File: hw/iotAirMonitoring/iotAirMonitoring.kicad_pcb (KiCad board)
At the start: 2 copper layers, 0 parts

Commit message: Schematic nearly finished
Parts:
- added C1: 100n, Capacitor_SMD:C_0402_1005Metric, F.Cu at (104.2, 81.4)
- added C10: 22u, Capacitor_SMD:C_0805_2012Metric, F.Cu at (112.0, 92.9)
- added C11: 100n/16V, Capacitor_SMD:C_0402_1005Metric, F.Cu at (106.8, 105.6)
- added C12: 47u/6V3, Capacitor_SMD:C_0805_2012Metric, F.Cu at (105.3, 98.6)
- added C13: 47u/6V3, Capacitor_SMD:C_0805_2012Metric, F.Cu at (112.0, 89.9)
- added C14: 22u, Capacitor_SMD:C_0805_2012Metric, F.Cu at (92.2, 106.9)
- added C15: 22u, Capacitor_SMD:C_0805_2012Metric, F.Cu at (112.0, 86.9)
- added C16: 4u7/16V, Capacitor_SMD:C_0603_1608Metric, F.Cu at (105.1, 101.4)
- added C17: 4u7/16V, Capacitor_SMD:C_0603_1608Metric, F.Cu at (109.6, 98.4)
- added C18: 10n/50V, Capacitor_SMD:C_0402_1005Metric, F.Cu at (106.8, 103.6)
- added C19: 1n, Capacitor_SMD:C_0402_1005Metric, F.Cu at (103.3, 107.6)
- added C2: 22u, Capacitor_SMD:C_0805_2012Metric, F.Cu at (100.5, 80.4)
- added C20: 47p, Capacitor_SMD:C_0402_1005Metric, F.Cu at (111.5, 100.6)
- added C21: 10n, Capacitor_SMD:C_0402_1005Metric, F.Cu at (113.0, 97.4)
- added C3: 100n, Capacitor_SMD:C_0402_1005Metric, F.Cu at (121.5, 76.4)
- added C4: 100n, Capacitor_SMD:C_0402_1005Metric, F.Cu at (132.7, 65.3)
- added C5: 100n, Capacitor_SMD:C_0402_1005Metric, F.Cu at (136.5, 60.7)
- added C6: 1n, Capacitor_SMD:C_0402_1005Metric, F.Cu at (118.5, 80.0)
- added C7: 100n, Capacitor_SMD:C_0402_1005Metric, F.Cu at (139.1, 58.8)
- added C8: 100n, Capacitor_SMD:C_0402_1005Metric, F.Cu at (107.1, 81.4)
- added C9: 22u, Capacitor_SMD:C_0805_2012Metric, F.Cu at (96.7, 106.9)
- added D1: LED, LED_SMD:LED_0805_2012Metric_Pad1.15x1.40mm_HandSolder, F.Cu at (96.1, 77.3)
- added D2: LED, LED_SMD:LED_0805_2012Metric_Pad1.15x1.40mm_HandSolder, F.Cu at (91.3, 77.3)
- added D3: LED, LED_SMD:LED_0805_2012Metric_Pad1.15x1.40mm_HandSolder, F.Cu at (86.5, 77.3)
- added D4: LED, LED_SMD:LED_0805_2012Metric_Pad1.15x1.40mm_HandSolder, F.Cu at (100.9, 77.3)
- added D5: SS54, Diode_SMD:D_SMA, F.Cu at (79.6, 105.7)
- added H1: MountingHole, MountingHole:MountingHole_3.2mm_M3_Pad_Via, F.Cu at (125.2, 87.0)
- added H2: MountingHole, MountingHole:MountingHole_3.2mm_M3_Pad_Via, F.Cu at (133.2, 87.0)
- added H3: MountingHole, MountingHole:MountingHole_3.2mm_M3_Pad_Via, F.Cu at (125.2, 95.0)
- added H4: MountingHole, MountingHole:MountingHole_3.2mm_M3_Pad_Via, F.Cu at (133.2, 95.0)
- added J1: MQ-7, Connector_PinSocket_2.54mm:PinSocket_1x04_P2.54mm_Vertical, F.Cu at (121.3, 45.6)
- added J10: USB_DATA, Connector_PinHeader_2.54mm:PinHeader_1x02_P2.54mm_Vertical, F.Cu at (107.4, 87.7)
- added J11: PWR, Connector_PinHeader_2.54mm:PinHeader_1x02_P2.54mm_Vertical, F.Cu at (96.3, 96.0)
- added J12: USB_B_Micro, Connector_USB:USB_Micro-B_Amphenol_10118194_Horizontal, F.Cu at (80.6, 99.0)
- added J2: VEML7700, Connector_PinSocket_2.54mm:PinSocket_1x05_P2.54mm_Vertical, F.Cu at (112.1, 45.6)
- added J3: SHT40, Connector_PinSocket_2.54mm:PinSocket_1x04_P2.54mm_Vertical, F.Cu at (116.7, 45.6)
- added J4: PROGRAMMER, Connector_PinHeader_2.54mm:PinHeader_1x06_P2.54mm_Vertical, F.Cu at (118.9, 85.3)
- added J5: ML8511, Connector_PinSocket_2.54mm:PinSocket_1x05_P2.54mm_Vertical, F.Cu at (107.5, 68.0)
- added J6: EN_3V3_PROGRAMMER, Connector_PinHeader_2.54mm:PinHeader_1x02_P2.54mm_Vertical, F.Cu at (139.4, 85.3)
- added J7: BMP388, Connector_PinSocket_2.54mm:PinSocket_1x08_P2.54mm_Vertical, F.Cu at (107.5, 45.6)
- added J9: USB_C_Receptacle_USB2.0, Connector_USB:USB_C_Receptacle_HRO_TYPE-C-31-M-12, F.Cu at (81.5, 91.2)
- added JP1: EN, Jumper:SolderJumper-2_P1.3mm_Open_RoundedPad1.0x1.5mm, F.Cu at (111.9, 79.8)
- added JP2: EN, Jumper:SolderJumper-2_P1.3mm_Open_RoundedPad1.0x1.5mm, F.Cu at (136.3, 53.6)
- added JP3: EN, Jumper:SolderJumper-2_P1.3mm_Open_RoundedPad1.0x1.5mm, F.Cu at (116.4, 75.2)
- added L1: 4u7, Inductor_SMD:L_Bourns-SRN6028, F.Cu at (101.1, 89.1)
- added Q1: MMBT3904, Package_TO_SOT_SMD:SOT-23, F.Cu at (127.0, 62.6)
- added Q10: AO3401A, Package_TO_SOT_SMD:SOT-23, F.Cu at (107.3, 94.9)
- added Q11: 2N7002, Package_TO_SOT_SMD:SOT-23, F.Cu at (100.9, 99.7)
- added Q12: AO3401A, Package_TO_SOT_SMD:SOT-23, F.Cu at (87.8, 104.6)
- added Q13: 2N7002, Package_TO_SOT_SMD:SOT-23, F.Cu at (96.2, 103.1)
- added Q2: MMBT3904, Package_TO_SOT_SMD:SOT-23, F.Cu at (122.5, 67.2)
- added Q3: AO3401A, Package_TO_SOT_SMD:SOT-23, F.Cu at (122.5, 62.6)
- added Q4: 2N7002, Package_TO_SOT_SMD:SOT-23, F.Cu at (112.0, 71.2)
- added Q5: AO3401A, Package_TO_SOT_SMD:SOT-23, F.Cu at (116.4, 71.2)
- added Q6: 2N7002, Package_TO_SOT_SMD:SOT-23, F.Cu at (112.0, 75.7)
- added Q7: AO3401A, Package_TO_SOT_SMD:SOT-23, F.Cu at (116.6, 57.8)
- added Q8: 2N7002, Package_TO_SOT_SMD:SOT-23, F.Cu at (121.0, 57.8)
- added Q9: AO3401A, Package_TO_SOT_SMD:SOT-23, F.Cu at (100.9, 95.2)
- added R1: R, Resistor_SMD:R_0805_2012Metric_Pad1.20x1.40mm_HandSolder, F.Cu at (91.2, 80.3)
- added R10: 10k, Resistor_SMD:R_0402_1005Metric, F.Cu at (129.8, 65.9)
- added R11: 220, Resistor_SMD:R_0402_1005Metric, F.Cu at (118.6, 78.0)
- added R12: 220, Resistor_SMD:R_0402_1005Metric, F.Cu at (122.9, 74.4)
- added R13: 100k, Resistor_SMD:R_0402_1005Metric, F.Cu at (133.6, 63.4)
- added R14: 3k3, Resistor_SMD:R_0402_1005Metric, F.Cu at (139.1, 56.8)
- added R15: 330, Resistor_SMD:R_0402_1005Metric, F.Cu at (126.2, 69.5)
- added R16: 3k3, Resistor_SMD:R_0402_1005Metric, F.Cu at (125.9, 71.5)
- added R17: 100k, Resistor_SMD:R_0402_1005Metric, F.Cu at (142.8, 54.8)
- added R18: 220, Resistor_SMD:R_0402_1005Metric, F.Cu at (139.9, 54.8)
- added R19: 220, Resistor_SMD:R_0402_1005Metric, F.Cu at (129.1, 69.5)
- added R2: R, Resistor_SMD:R_0805_2012Metric_Pad1.20x1.40mm_HandSolder, F.Cu at (95.9, 80.3)
- added R20: 100k, Resistor_SMD:R_0402_1005Metric, F.Cu at (142.8, 52.8)
- added R21: R, Resistor_SMD:R_0805_2012Metric_Pad1.20x1.40mm_HandSolder, F.Cu at (86.4, 80.3)
- added R22: 100k, Resistor_SMD:R_0402_1005Metric, F.Cu at (115.6, 80.0)
- added R23: 220, Resistor_SMD:R_0402_1005Metric, F.Cu at (123.0, 72.5)
- added R24: 100k, Resistor_SMD:R_0402_1005Metric, F.Cu at (115.7, 78.0)
- added R25: 100k, Resistor_SMD:R_0402_1005Metric, F.Cu at (123.0, 70.5)
- added R26: 100k, Resistor_SMD:R_0402_1005Metric, F.Cu at (120.0, 74.5)
- added R27: 5k1, Resistor_SMD:R_0402_1005Metric, F.Cu at (100.4, 105.5)
- added R28: 5k1, Resistor_SMD:R_0402_1005Metric, F.Cu at (111.0, 95.4)
- added R29: 100k, Resistor_SMD:R_0402_1005Metric, F.Cu at (113.9, 95.4)
- added R3: 1k, Resistor_SMD:R_0402_1005Metric, F.Cu at (120.1, 72.5)
- added R30: 100k, Resistor_SMD:R_0402_1005Metric, F.Cu at (103.3, 105.6)
- added R31: 10k, Resistor_SMD:R_0402_1005Metric, F.Cu at (108.6, 101.1)
- added R32: 100k, Resistor_SMD:R_0402_1005Metric, F.Cu at (103.9, 103.7)
- added R33: 100k, Resistor_SMD:R_0402_1005Metric, F.Cu at (100.4, 107.5)
- added R34: 15k, Resistor_SMD:R_0402_1005Metric, F.Cu at (91.5, 103.3)
- added R35: 4k7, Resistor_SMD:R_0402_1005Metric, F.Cu at (88.8, 94.6)
- added R36: 100k, Resistor_SMD:R_0402_1005Metric, F.Cu at (91.7, 94.6)
- added R37: 30k, Resistor_SMD:R_0603_1608Metric, F.Cu at (100.5, 103.3)
- added R4: 1k, Resistor_SMD:R_0402_1005Metric, F.Cu at (139.9, 52.8)
- added R5: 1k, Resistor_SMD:R_0402_1005Metric, F.Cu at (111.2, 59.0)
- added R6: 10k, Resistor_SMD:R_0402_1005Metric, F.Cu at (130.7, 63.4)
- added R7: 220, Resistor_SMD:R_0402_1005Metric, F.Cu at (130.7, 61.4)
- added R8: 10k, Resistor_SMD:R_0402_1005Metric, F.Cu at (133.6, 61.4)
- added R9: 220, Resistor_SMD:R_0402_1005Metric, F.Cu at (120.1, 70.5)
- added SW1: SW_Push, Button_Switch_THT:SW_PUSH_6mm, F.Cu at (111.8, 62.4)
- added SW2: SW_Push, Button_Switch_THT:SW_PUSH_6mm, F.Cu at (125.6, 53.8)
- added SW3: RESET, Button_Switch_THT:SW_PUSH_6mm, F.Cu at (125.6, 45.3)
- added SW4: SW_Push, Button_Switch_THT:SW_PUSH_6mm, F.Cu at (136.1, 45.3)
- added TP1: TP_SDA, TestPoint:TestPoint_Pad_D1.5mm, F.Cu at (126.5, 66.7)
- added TP2: TP_SCL, TestPoint:TestPoint_Pad_D1.5mm, F.Cu at (135.9, 57.1)
- added U1: ESP32-WROOM-32, RF_Module:ESP32-WROOM-32, F.Cu at (90.4, 64.8)
- added U2: MCP3202-BI/SN, Package_SO:SOIC-8_3.9x4.9mm_P1.27mm, F.Cu at (79.8, 79.0)
- added U3: AMS1117-3.3, Package_TO_SOT_SMD:SOT-223-3_TabPin2, F.Cu at (92.2, 89.5)
- added U4: TPS54331, Package_SO:SOIC-8_3.9x4.9mm_P1.27mm, F.Cu at (89.8, 99.1)

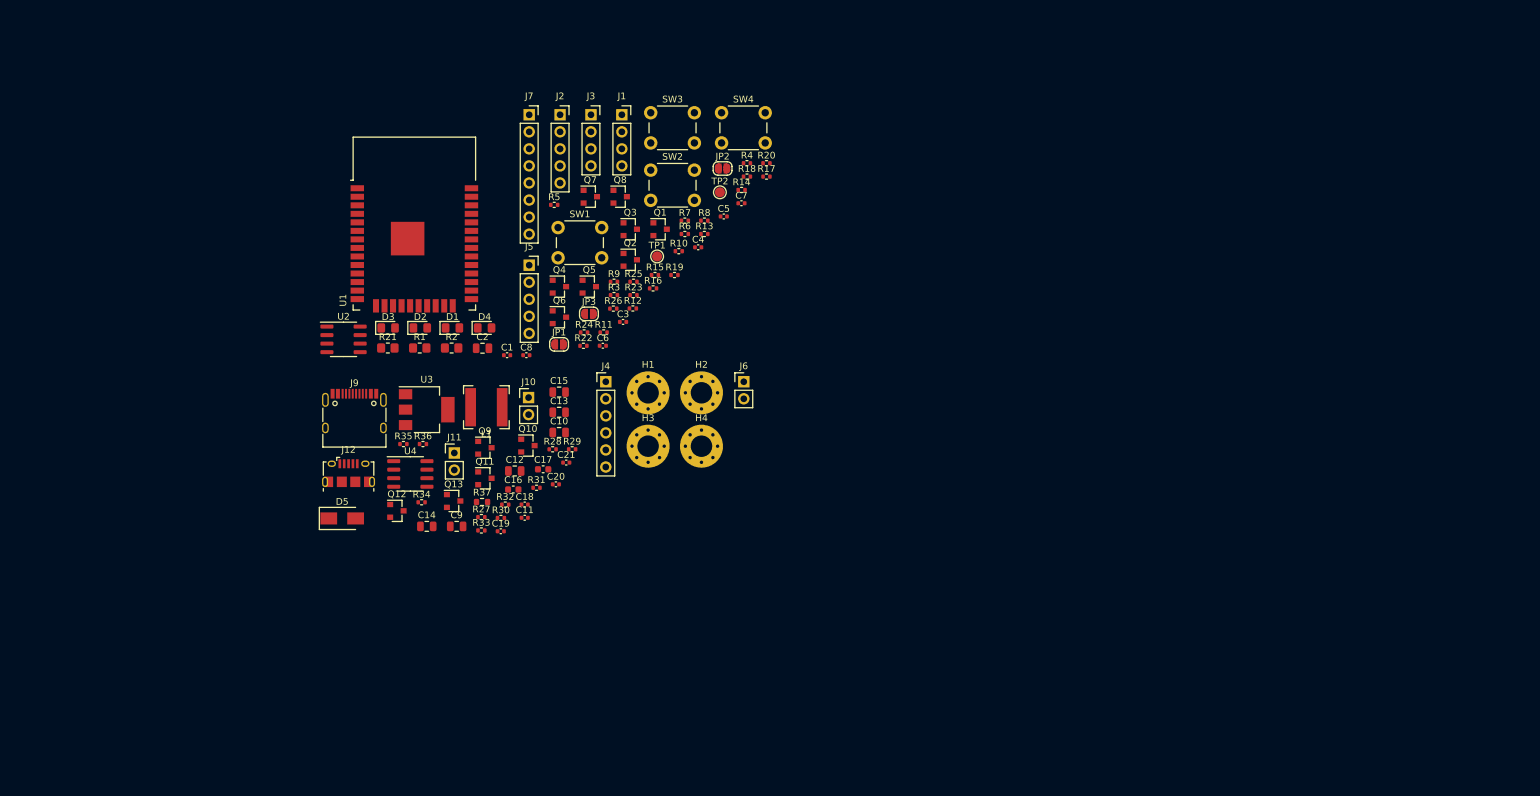
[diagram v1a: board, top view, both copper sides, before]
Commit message: Start routing main board
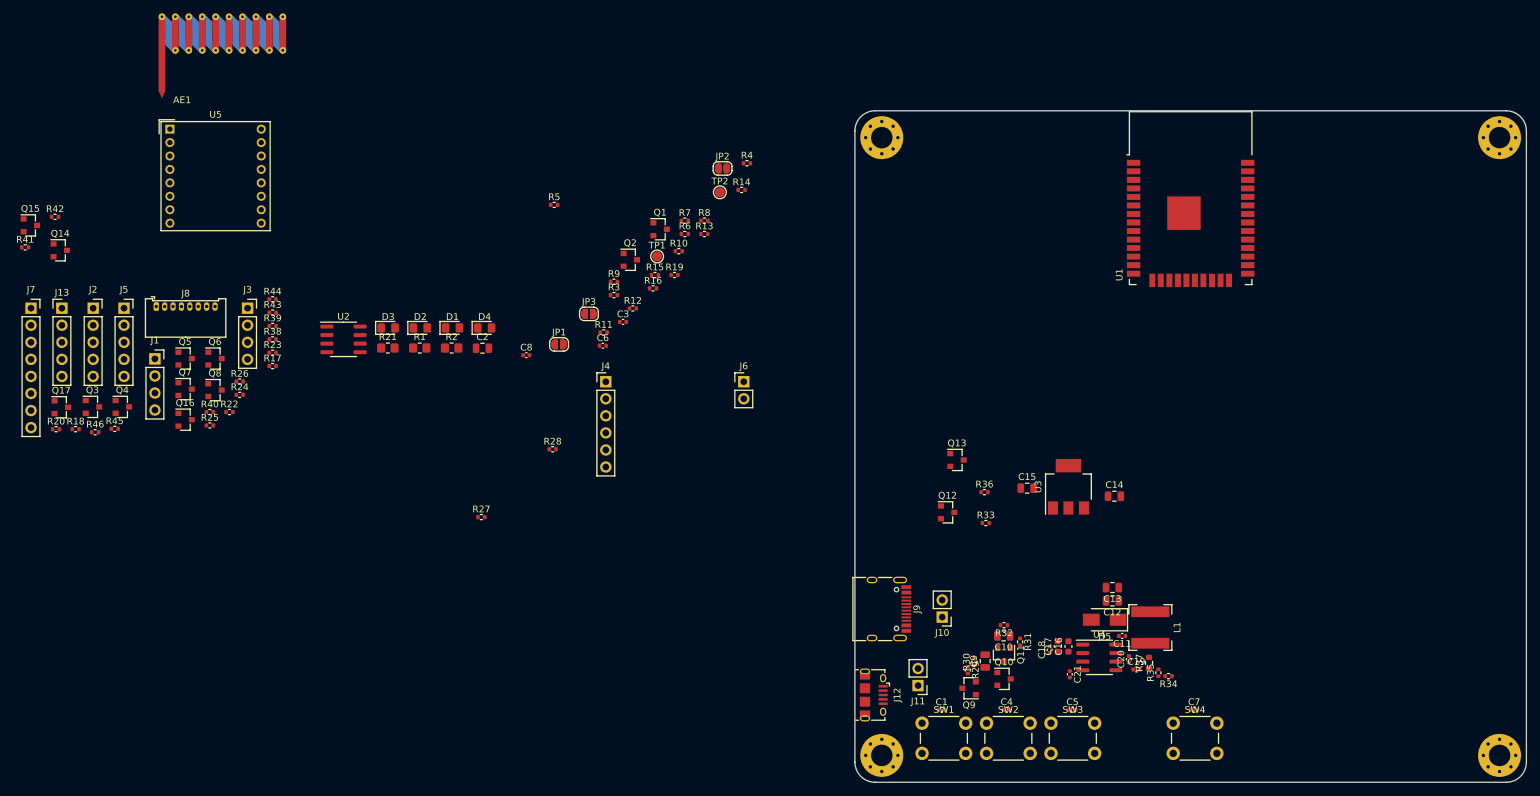
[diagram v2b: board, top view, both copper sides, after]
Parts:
- added AE1: Antenna, RF_Antenna:Texas_SWRA416_868MHz_915MHz, F.Cu at (61.8, 36.8)
- added J13: PM1003, Connector_PinHeader_2.54mm:PinHeader_1x05_P2.54mm_Vertical, F.Cu at (37.9, 74.4)
- added J8: PMS5003, Connector_Molex:Molex_PicoBlade_53048-0810_1x08_P1.25mm_Horizontal, F.Cu at (52.0, 74.2)
- added Q14: AO3401A, Package_TO_SOT_SMD:SOT-23, F.Cu at (37.6, 65.8)
- added Q15: 2N7002, Package_TO_SOT_SMD:SOT-23, F.Cu at (33.2, 62.1)
- added Q16: 2N7002, Package_TO_SOT_SMD:SOT-23, F.Cu at (56.2, 91.0)
- added Q17: 2N7002, Package_TO_SOT_SMD:SOT-23, F.Cu at (37.8, 89.2)
- added R38: 100k, Resistor_SMD:R_0402_1005Metric, F.Cu at (69.3, 79.0)
- added R39: 100k, Resistor_SMD:R_0402_1005Metric, F.Cu at (69.3, 77.0)
- added R40: 100k, Resistor_SMD:R_0402_1005Metric, F.Cu at (59.9, 89.9)
- added R41: 100k, Resistor_SMD:R_0402_1005Metric, F.Cu at (32.4, 65.3)
- added R42: 100k, Resistor_SMD:R_0402_1005Metric, F.Cu at (36.9, 60.8)
- added R43: 100k, Resistor_SMD:R_0402_1005Metric, F.Cu at (69.3, 75.1)
- added R44: 100k, Resistor_SMD:R_0402_1005Metric, F.Cu at (69.3, 73.1)
- added R45: 100k, Resistor_SMD:R_0402_1005Metric, F.Cu at (45.8, 92.4)
- added R46: 100k, Resistor_SMD:R_0402_1005Metric, F.Cu at (42.9, 92.9)
- added U5: RFM95W-868S2, RF_Module:HOPERF_RFM9XW_THT, F.Cu at (54.0, 47.7)
- SW1: value SW_Push -> PWR_ON
- SW2: value SW_Push -> PWR_OFF
- moved H4 127.5 mm to (252.0, 141.0)
- moved H2 124.8 mm to (252.0, 49.0)
- moved R35 117.5 mm to (201.2, 128.7), turned to 90 degrees
- moved U1 115.7 mm to (206.0, 61.0)
- moved D5 114.6 mm to (193.2, 120.8), turned to 180 degrees
- moved R34 114.2 mm to (202.7, 129.2), turned to 180 degrees
- moved SW4 113.1 mm to (203.4, 136.2)
- moved R20 113.0 mm to (37.0, 92.4)
- moved SW3 108.7 mm to (185.2, 136.2)
- moved R18 106.8 mm to (39.9, 92.4)
- moved U4 106.2 mm to (192.4, 126.4)
- moved L1 104.2 mm to (200.0, 122.0), turned to 90 degrees
- moved C14 102.5 mm to (194.7, 102.4)
- moved R37 102.2 mm to (199.8, 127.2), turned to 90 degrees
- moved C7 101.2 mm to (206.5, 134.2)
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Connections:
- net /MQ_7-VDD renamed MQ-7_VDD
- J5 pad 1: UV_EN -> /interface/UV_EN
- Q7 pad 3: Net-(J8-Pad1) -> DUST_VDD
- R24 pad 1: Net-(Q6-Pad1) -> 3V3
- R24 pad 2: GND -> /interface/UV_EN
- R25 pad 1: VDD -> Net-(Q6-Pad1)
- R25 pad 2: Net-(Q7-Pad1) -> GND
- R26 pad 1: PMS_EN -> VDD
- R26 pad 2: GND -> Net-(Q7-Pad1)
- U1 pad 13: Net-(U1-Pad13) -> LORA_EN
- U1 pad 14: Net-(U1-Pad14) -> CS_LORA
- U1 pad 23: Net-(U1-Pad23) -> LED
- U1 pad 5: Net-(U1-Pad5) -> DIO1
- U1 pad 8: LED -> LORA_RST
- U1 pad 9: Net-(U1-Pad9) -> DIO0
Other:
- board outline added: 100 x 100 mm
- rule trace_min: 0.2 -> 0.15
- rule via_min_size: 0.4 -> 0.6

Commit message: More component placement
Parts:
- moved R20 124.1 mm to (161.0, 85.9), turned to 270 degrees
- moved Q3 121.1 mm to (163.4, 82.4), turned to 180 degrees
- moved Q4 116.5 mm to (163.4, 86.0)
- moved J5 116.0 mm to (158.2, 107.8), turned to 180 degrees
- moved J1 106.5 mm to (158.2, 82.4)
- moved D3 106.2 mm to (186.6, 112.8), turned to 90 degrees
- moved R13 100.2 mm to (204.5, 134.2)
- moved R24 99.3 mm to (161.5, 107.8), turned to 180 degrees
- moved U2 98.4 mm to (176.0, 100.0)
- moved R17 96.5 mm to (165.8, 82.3), turned to 270 degrees
- moved R5 90.6 mm to (186.6, 109.2), turned to 270 degrees
- moved JP3 76.9 mm to (186.6, 106.5), turned to 270 degrees
- moved R27 67.0 mm to (166.4, 116.7), turned to 270 degrees
- moved R28 61.3 mm to (166.4, 121.5), turned to 90 degrees
- moved Q13 23.1 mm to (178.8, 118.8), turned to 270 degrees
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
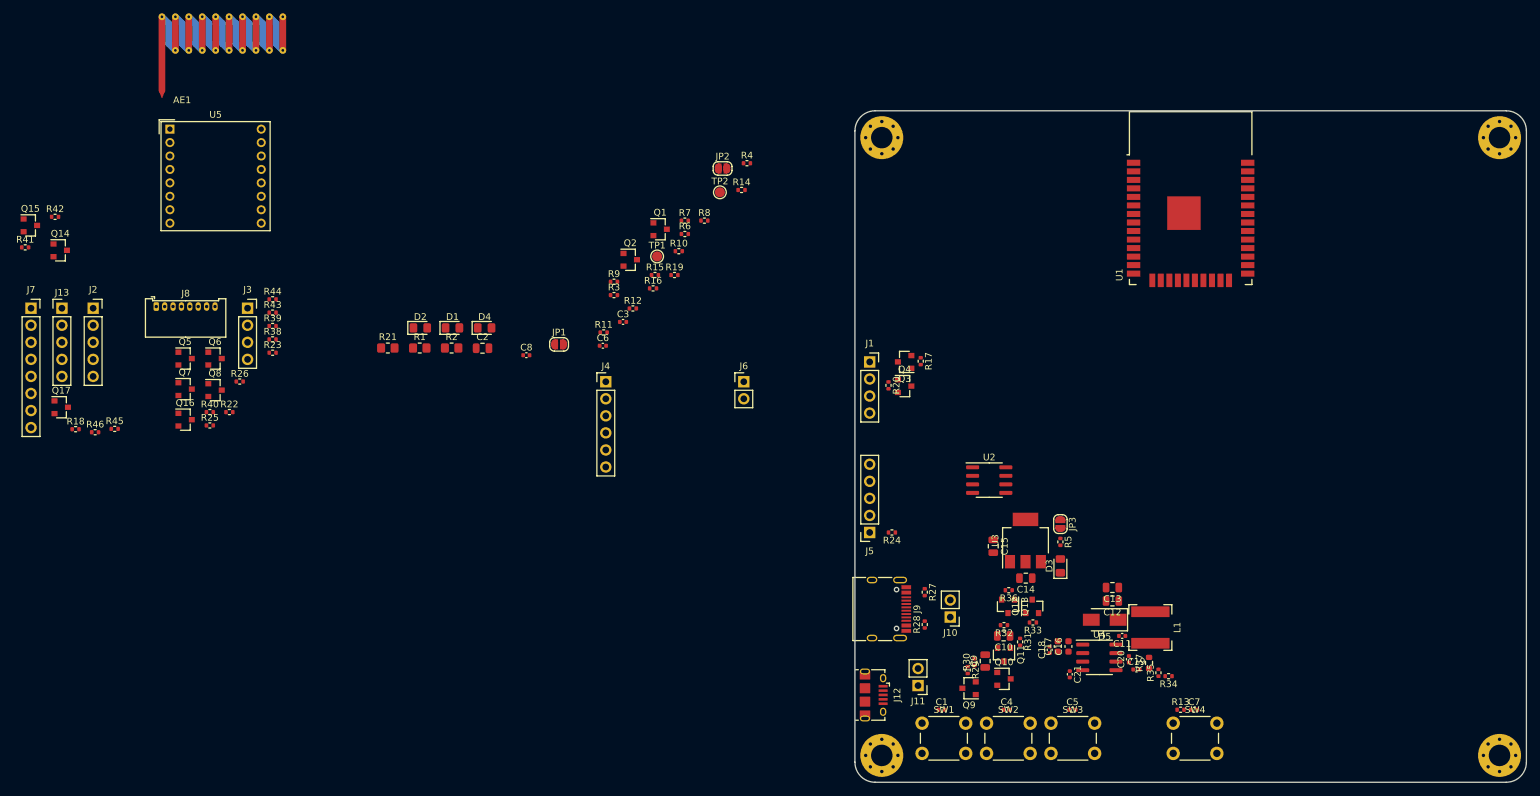
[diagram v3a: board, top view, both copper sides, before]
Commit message: Nearly finished component placement
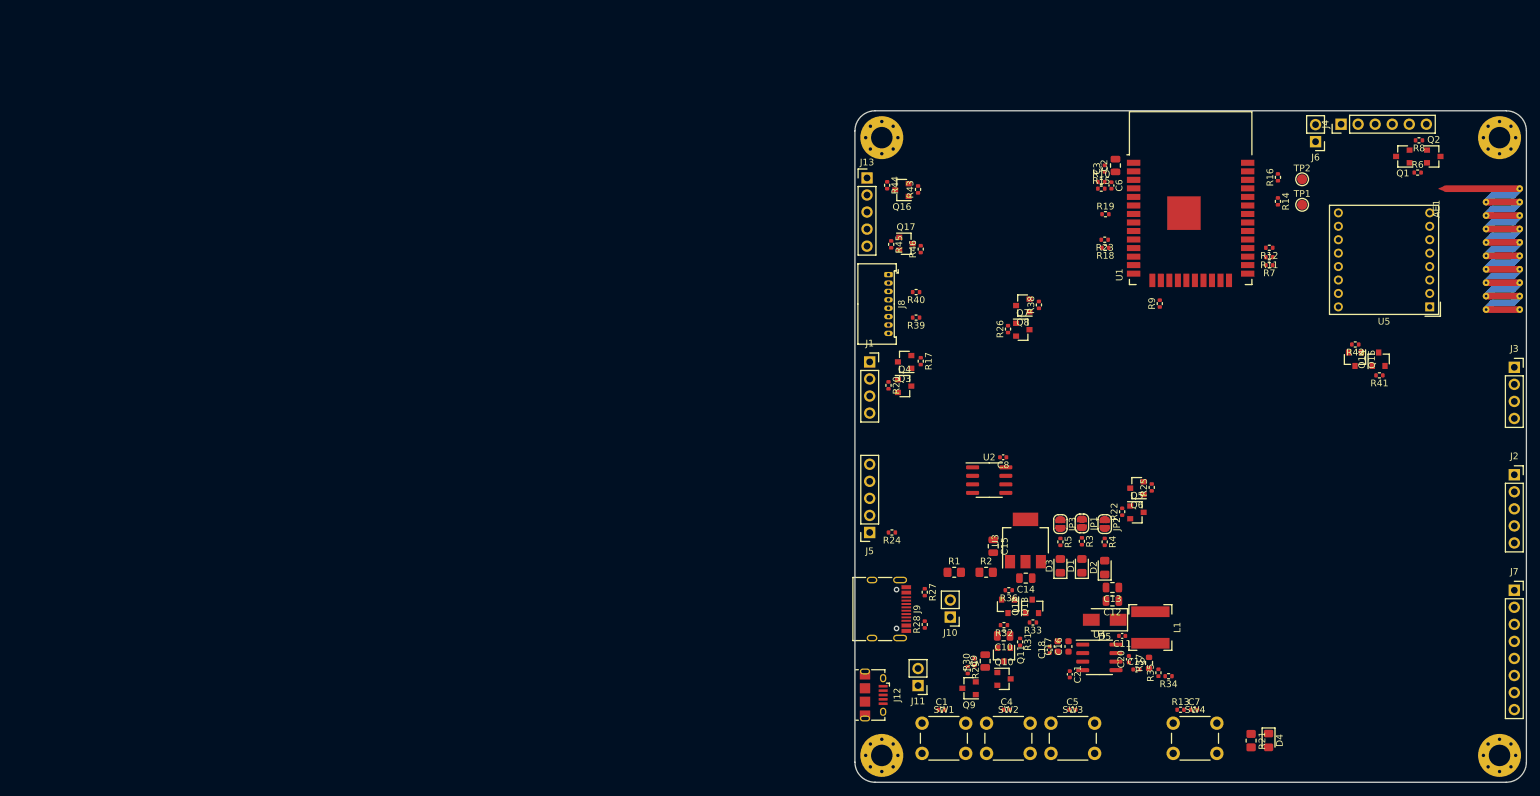
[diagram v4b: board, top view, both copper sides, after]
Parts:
- moved J7 224.9 mm to (254.2, 116.4)
- moved J2 213.1 mm to (254.2, 99.2)
- moved R41 202.6 mm to (234.1, 84.4), turned to 180 degrees
- moved Q15 198.3 mm to (230.5, 82.0), turned to 270 degrees
- moved Q14 197.0 mm to (234.0, 82.0), turned to 90 degrees
- moved R42 194.6 mm to (230.5, 79.8), turned to 180 degrees
- moved AE1 189.6 mm to (249.2, 65.6), turned to 270 degrees
- moved U5 189.5 mm to (241.6, 74.2), turned to 180 degrees
- moved J3 188.9 mm to (254.2, 83.2)
- moved R18 155.7 mm to (193.3, 65.4), turned to 180 degrees
- moved Q5 143.6 mm to (198.0, 104.8)
- moved R21 141.2 mm to (215.0, 138.8), turned to 270 degrees
- moved R25 140.6 mm to (200.2, 101.1), turned to 90 degrees
- moved Q6 138.6 mm to (198.0, 101.2), turned to 180 degrees
- moved R22 133.8 mm to (195.8, 104.7), turned to 90 degrees
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
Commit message: Start routing of main board
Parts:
- moved J10 2.21 mm to (170.4, 118.2), turned to 0 degrees
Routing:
- net USB_VDD: track 0.00 -> 29.1 mm
- net 3V3_L: track 0.00 -> 23.8 mm
- net ADC_0: track 0.00 -> 19.2 mm
- net ADC_1: track 0.00 -> 17.2 mm
- net D+: track 0.00 -> 15.8 mm, vias 0 -> 2
- net GND: track 0.00 -> 14.6 mm
- net PWR_OFF: track 0.00 -> 14.3 mm
- net D-: track 0.00 -> 13.1 mm, vias 0 -> 2
- net PWR_ON: track 0.00 -> 12.6 mm
- net Net-(C5-Pad1): track 0.00 -> 10.8 mm
- net SWITCH: track 0.00 -> 10.2 mm
- net SCL: track 0.00 -> 8.25 mm
- net SDA: track 0.00 -> 8.14 mm
- net 3V3: track 0.00 -> 8.14 mm
- net VSNS: track 0.00 -> 7.70 mm
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- added copper zone on F.Cu, net 3V3_L
- added copper zone on F.Cu, net Net-(C11-Pad1)
- added copper zone on F.Cu, net Net-(C14-Pad1)
- added copper zone on F.Cu, net VDD
